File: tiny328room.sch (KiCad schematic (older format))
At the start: 12 parts, among them K1 PIR, U1 DS18B20, U2 DHT11, U3 TINY328

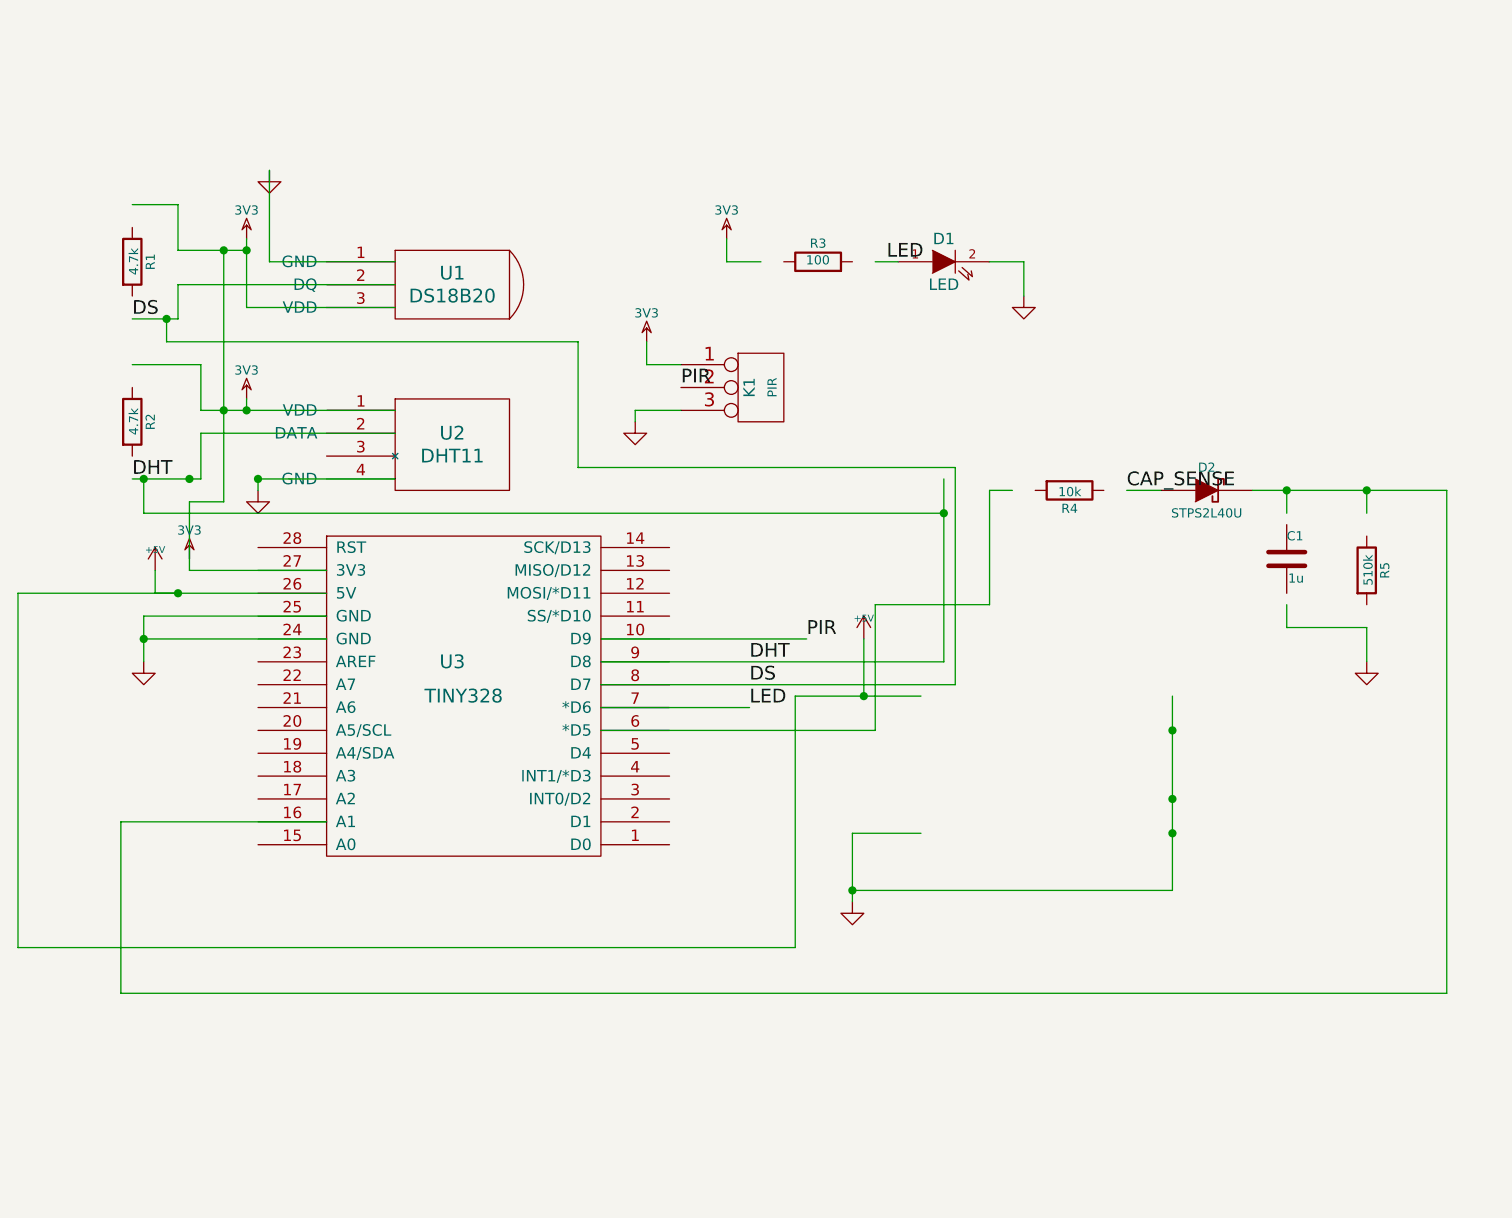
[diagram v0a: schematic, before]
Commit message: add ambient light sensor
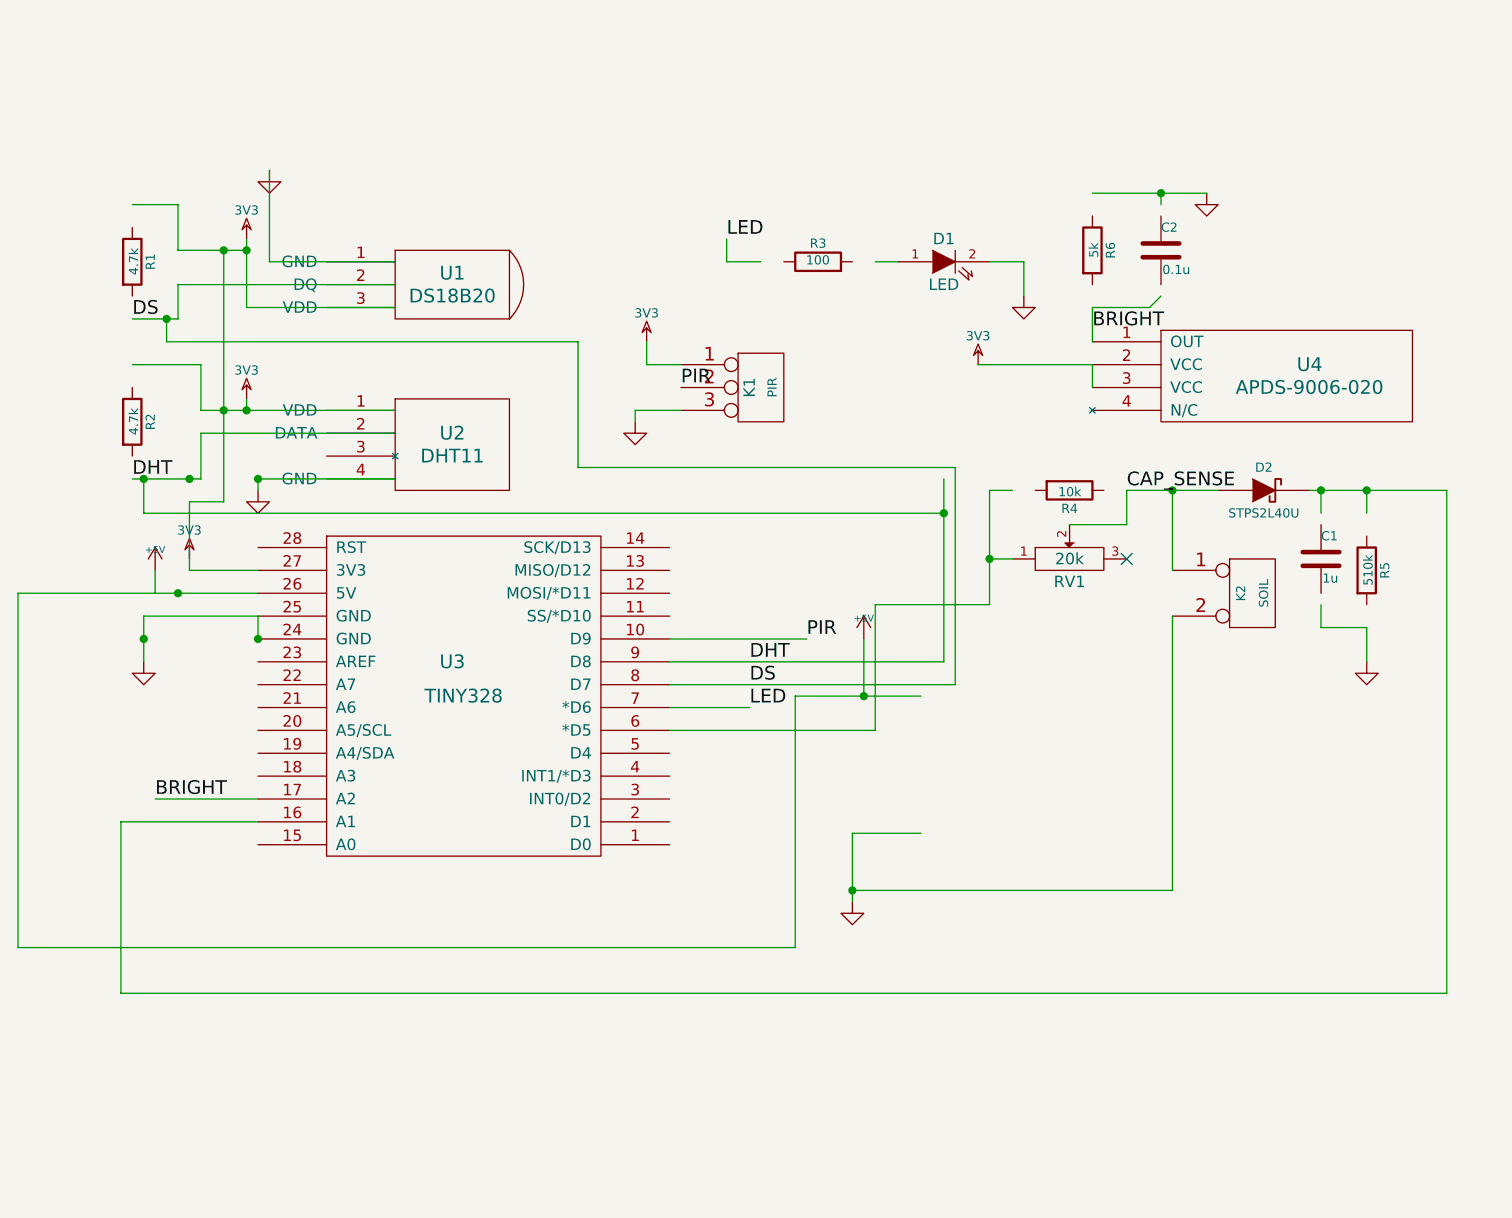
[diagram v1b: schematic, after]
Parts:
- added C2: 0.1u, ~, symbol C
- added K2: SOIL, ~, symbol CONN_2
- added R6: 5k, ~, symbol R
- added RV1: 20k, ~, symbol POT
- added U4: APDS-9006-020, symbol APDS-9006-020
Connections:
- net labels added: BRIGHT
- wire segments 75 -> 86
- no-connect marks 0 -> 1
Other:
- moved on the sheet: C1, D2
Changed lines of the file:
@@
 Sheet 1 1
 Title ""
-Date "3 nov 2014"
+Date "22 feb 2015"
 Rev ""
 Comp ""
@@
 $EndComp
 $Comp
-L GND #PWR11
+L GND #PWR10
 U 1 1 5454FBFF
 P 6300 5200
-F 0 "#PWR11" H 6300 5200 30  0001 C CNN
+F 0 "#PWR10" H 6300 5200 30  0001 C CNN
 F 1 "GND" H 6300 5130 30  0001 C CNN
 F 2 "" H 6300 5200 60  0000 C CNN
@@
 	6350 4300 6350 4050
 $Comp
-L +5V #PWR12
+L +5V #PWR11
 U 1 1 5454FC2C
 P 6350 4050
-F 0 "#PWR12" H 6350 4140 20  0001 C CNN
+F 0 "#PWR11" H 6350 4140 20  0001 C CNN
 F 1 "+5V" H 6350 4140 30  0000 C CNN
 F 2 "" H 6350 4050 60  0000 C CNN
@@
 Wire Wire Line
 	3250 3750 3250 3850
-Wire Wire Line
-	3250 3850 4000 3850
 $Comp
 L GND #PWR1
@@
 Wire Wire Line
 	3200 3950 3200 4150
-Wire Wire Line
-	3200 4050 4000 4050
-Wire Wire Line
-	3200 3950 4000 3950
 Connection ~ 3200 4050
 $Comp
@@
 Wire Wire Line
 	3400 3450 3400 3750
-Wire Wire Line
-	3400 3750 4000 3750
 $Comp
 L 3V3 #PWR5
@@
 Connection ~ 3700 3350
 Wire Wire Line
-	3450 3150 3450 3350
-Wire Wire Line
-	3450 3350 3150 3350
+	3450 3350 3450 3150
+Wire Wire Line
+	3150 3350 3450 3350
 Wire Wire Line
 	3700 3350 4300 3350
@@
 	3350 2500 4300 2500
 Wire Wire Line
-	3350 2500 3350 2650
-Wire Wire Line
-	3350 2650 3150 2650
+	3350 2650 3350 2500
+Wire Wire Line
+	3150 2650 3350 2650
 Wire Wire Line
 	3150 2150 3350 2150
@@
 DHT
 Wire Wire Line
-	7700 4300 7700 5150
-Connection ~ 7700 4750
-Connection ~ 7700 4450
+	7700 3950 7700 5150
 Wire Wire Line
 	7700 5150 6300 5150
 Connection ~ 6300 5150
-Connection ~ 7700 4900
 $Comp
 L R R3
@@
 	0    -1   -1   0
 $EndComp
-$Comp
-L 3V3 #PWR10
-U 1 1 5454FF6A
-P 5750 2300
-F 0 "#PWR10" H 5750 2400 40  0001 C CNN
-F 1 "3V3" H 5750 2425 40  0000 C CNN
-F 2 "" H 5750 2300 60  0000 C CNN
-F 3 "" H 5750 2300 60  0000 C CNN
-	1    5750 2300
-	1    0    0    -1
-$EndComp
 Wire Wire Line
 	5750 2300 5750 2400
@@
 Wire Wire Line
 	7050 2400 6900 2400
-Text Label 6450 2400 0    60   ~ 0
+Text Label 5750 2300 0    60   ~ 0
 LED
 Text Label 5550 2950 0    60   ~ 0
@@
 PIR
 Wire Wire Line
-	5200 4350 5850 4350
-Wire Wire Line
-	5200 4250 6750 4250
-Wire Wire Line
-	5200 4150 6700 4150
-Wire Wire Line
-	5200 4050 6100 4050
-Wire Wire Line
 	3550 3450 3400 3450
 Wire Wire Line
@@
 Connection ~ 3550 2350
 Wire Wire Line
-	6700 4150 6700 3350
+	6700 3350 6700 4150
 Connection ~ 3400 3350
 Wire Wire Line
@@
 	2650 5400 2650 3850
 Wire Wire Line
-	2650 3850 3350 3850
+	2650 3850 3700 3850
 Connection ~ 3350 3850
 Connection ~ 6350 4300
@@
 L DIODESCH D2
 U 1 1 54565051
-P 7850 3400
-F 0 "D2" H 7850 3500 40  0000 C CNN
-F 1 "STPS2L40U" H 7850 3300 40  0000 C CNN
-F 2 "" H 7850 3400 60  0000 C CNN
-F 3 "" H 7850 3400 60  0000 C CNN
-	1    7850 3400
+P 8100 3400
+F 0 "D2" H 8100 3500 40  0000 C CNN
+F 1 "STPS2L40U" H 8100 3300 40  0000 C CNN
+F 2 "" H 8100 3400 60  0000 C CNN
+F 3 "" H 8100 3400 60  0000 C CNN
+	1    8100 3400
 	1    0    0    -1
 $EndComp
@@
 L C C1
 U 1 1 545650C0
-P 8200 3700
-F 0 "C1" H 8200 3800 40  0000 L CNN
-F 1 "1u" H 8206 3615 40  0000 L CNN
-F 2 "~" H 8238 3550 30  0000 C CNN
-F 3 "" H 8200 3700 60  0000 C CNN
-	1    8200 3700
+P 8350 3700
+F 0 "C1" H 8350 3800 40  0000 L CNN
+F 1 "1u" H 8356 3615 40  0000 L CNN
+F 2 "~" H 8388 3550 30  0000 C CNN
+F 3 "" H 8350 3700 60  0000 C CNN
+	1    8350 3700
 	1    0    0    -1
 $EndComp
@@
 $EndComp
 $Comp
-L GND #PWR14
+L GND #PWR15
 U 1 1 545651E6
 P 8550 4150
-F 0 "#PWR14" H 8550 4150 30  0001 C CNN
+F 0 "#PWR15" H 8550 4150 30  0001 C CNN
 F 1 "GND" H 8550 4080 30  0001 C CNN
 F 2 "" H 8550 4150 60  0000 C CNN
@@
 	8550 4150 8550 4000
 Wire Wire Line
-	8550 4000 8200 4000
-Wire Wire Line
-	8200 4000 8200 3900
-Wire Wire Line
-	8050 3400 8900 3400
-Wire Wire Line
-	8200 3400 8200 3500
-Wire Wire Line
 	8550 3400 8550 3500
-Connection ~ 8200 3400
-Wire Wire Line
-	7650 3400 7500 3400
+Wire Wire Line
+	7500 3400 7900 3400
 Wire Wire Line
 	7000 3400 6900 3400
@@
 	6400 3900 6400 4450
 Wire Wire Line
-	6400 4450 5200 4450
-Wire Wire Line
 	8900 3400 8900 5600
 Wire Wire Line
@@
 Wire Wire Line
 	3100 5600 3100 4850
-Wire Wire Line
-	3100 4850 4000 4850
 Connection ~ 8550 3400
 Text Label 7500 3400 0    60   ~ 0
 CAP_SENSE
+$Comp
+L POT RV1
+U 1 1 545D15F2
+P 7250 3700
+F 0 "RV1" H 7250 3600 50  0000 C CNN
+F 1 "20k" H 7250 3700 50  0000 C CNN
+F 2 "~" H 7250 3700 60  0000 C CNN
+F 3 "~" H 7250 3700 60  0000 C CNN
+	1    7250 3700
+	1    0    0    -1
+$EndComp
+Wire Wire Line
+	8350 3500 8350 3400
+Connection ~ 8350 3400
+Wire Wire Line
+	8300 3400 8900 3400
+Wire Wire Line
+	8350 3900 8350 4000
+Wire Wire Line
+	8350 4000 8550 4000
+Wire Wire Line
+	6900 3700 7000 3700
+Connection ~ 6900 3700
+Wire Wire Line
+	7250 3550 7500 3550
+Wire Wire Line
+	7500 3550 7500 3400
+NoConn ~ 7500 3700
+Connection ~ 3700 4050
+Wire Wire Line
+	3700 3950 3700 4050
+Wire Wire Line
+	3700 3950 3200 3950
+Wire Wire Line
+	3400 3750 3700 3750
+Wire Wire Line
+	5500 4050 6100 4050
+Wire Wire Line
+	6700 4150 5500 4150
+Wire Wire Line
+	6750 4250 5500 4250
+Wire Wire Line
+	5500 4350 5850 4350
+Wire Wire Line
+	6400 4450 5500 4450
+Wire Wire Line
+	3100 4850 3700 4850
+$Comp
+L CONN_2 K2
+U 1 1 545D2BDC
+P 8050 3850
+F 0 "K2" V 8000 3850 40  0000 C CNN
+F 1 "SOIL" V 8100 3850 40  0000 C CNN
+F 2 "~" H 8050 3850 60  0000 C CNN
+F 3 "~" H 8050 3850 60  0000 C CNN
+	1    8050 3850
+	1    0    0    -1
+$EndComp
+Wire Wire Line
+	7700 3750 7700 3400
+Connection ~ 7700 3400
+$Comp
+L APDS-9006-020 U4
+U 1 1 54E9BE88
+P 8200 2900
+F 0 "U4" H 8300 2950 60  0000 C CNN
+F 1 "APDS-9006-020" H 8300 2850 60  0000 C CNN
+F 2 "" H 8350 2950 60  0000 C CNN
+F 3 "" H 8350 2950 60  0000 C CNN
+	1    8200 2900
+	1    0    0    -1
+$EndComp
+$Comp
+L 3V3 #PWR12
+U 1 1 54E9BEC9
+P 6850 2850
+F 0 "#PWR12" H 6850 2950 40  0001 C CNN
+F 1 "3V3" H 6850 2975 40  0000 C CNN
+F 2 "" H 6850 2850 60  0000 C CNN
+F 3 "" H 6850 2850 60  0000 C CNN
+	1    6850 2850
+	1    0    0    -1
+$EndComp
+Wire Wire Line
+	6850 2850 7350 2850
+Wire Wire Line
+	7350 2850 7350 2950
+$Comp
+L R R6
+U 1 1 54E9BF9B
+P 7350 2350
+F 0 "R6" V 7430 2350 40  0000 C CNN
+F 1 "5k" V 7357 2351 40  0000 C CNN
+F 2 "~" V 7280 2350 30  0000 C CNN
+F 3 "~" H 7350 2350 30  0000 C CNN
+	1    7350 2350
+	1    0    0    -1
+$EndComp
+Wire Wire Line
+	7350 2600 7350 2750
+$Comp
+L GND #PWR14
+U 1 1 54E9C00D
+P 7850 2100
+F 0 "#PWR14" H 7850 2100 30  0001 C CNN
+F 1 "GND" H 7850 2030 30  0001 C CNN
+F 2 "" H 7850 2100 60  0000 C CNN
+F 3 "" H 7850 2100 60  0000 C CNN
+	1    7850 2100
+	1    0    0    -1
+$EndComp
+Wire Wire Line
+	7850 2100 7350 2100
+Text Label 7350 2700 0    60   ~ 0
+BRIGHT
+Text Label 3250 4750 0    60   ~ 0
+BRIGHT
+Wire Wire Line
+	3250 4750 3700 4750
+$Comp
+L C C2
+U 1 1 54E9C2BB
+P 7650 2350
+F 0 "C2" H 7650 2450 40  0000 L CNN
+F 1 "0.1u" H 7656 2265 40  0000 L CNN
+F 2 "~" H 7688 2200 30  0000 C CNN
+F 3 "~" H 7650 2350 60  0000 C CNN
+	1    7650 2350
+	1    0    0    -1
+$EndComp
+Wire Wire Line
+	7350 2600 7600 2600
+Wire Wire Line
+	7600 2600 7650 2550
+Wire Wire Line
+	7650 2150 7650 2100
+Connection ~ 7650 2100
 $EndSCHEMATC
